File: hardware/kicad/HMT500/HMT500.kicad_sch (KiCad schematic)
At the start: 0 parts

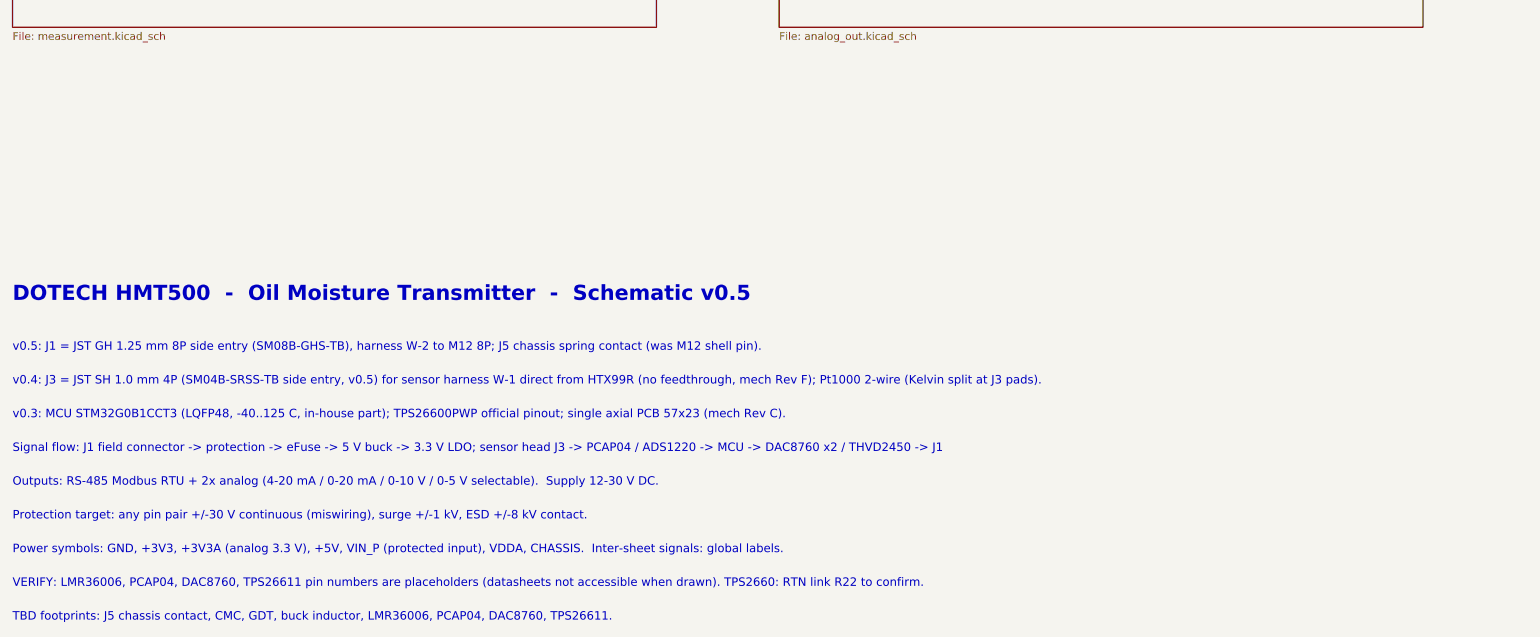
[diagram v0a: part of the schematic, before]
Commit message: Schematic drawing rules: no overlapping text, Korean font, distinct net names
- Generator places reference/value text automatically, clear of symbol bodies,
  pins, wires, labels, notes and box edges; validation fails on any overlap
  (also note text vs wires/power names and bodies vs box edges)
- Fix 180-degree parts (LED) whose justification KiCad mirrors
- Styles: reference bold, value normal, power nets italic, signal nets boxed labels
- Korean box subtitles and legend in NanumGothic TrueType (stroke font has no Hangul)
- Nets renamed where they matched part or pin names: LED -> STAT_LED, EF_ILIM/IMON/DVDT
- J1 GH mounting pads removed from the symbol (PCB only); connector sheet re-spaced
- Schematic PDF export added; tests for net naming and Hangul font

Co-Authored-By: Claude Opus 5.5 <noreply@anthropic.com>
Claude-Session: https://claude.ai/code/session_01JA2o8uJsqp9Vzsg4b665ev
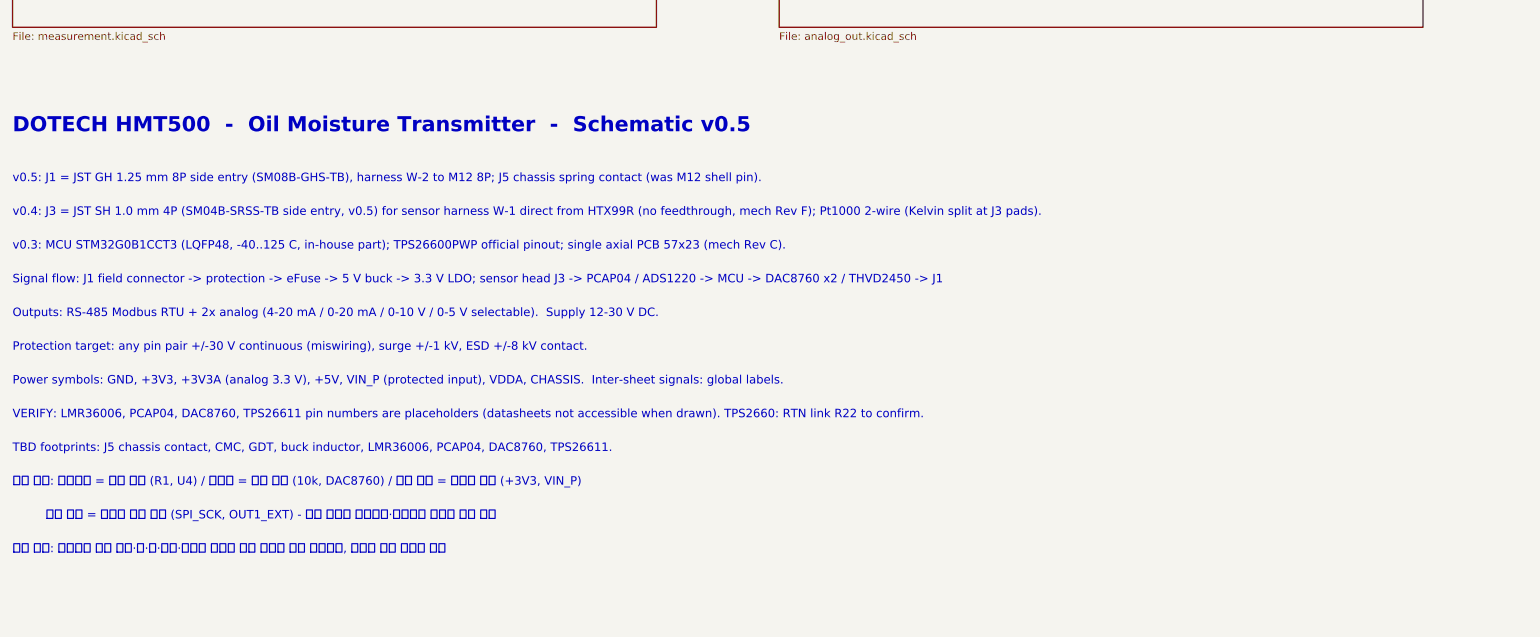
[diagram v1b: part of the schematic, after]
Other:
- note added: "글자 겹침: 생성기가 부품 몸체·핀·선·라벨·메모와 겹치지 않는 자리에 자동 배치하고, 겹치면 생성 실패로 처리"
- note added: "신호 네트 = 테두리 있는 라벨 (SPI_SCK, OUT1_EXT) - 네트 이름은 부품번호·부품명과 겹치지 않게 지음"
- note added: "표기 규칙: 부품번호 = 굵은 글자 (R1, U4) / 부품값 = 보통 글자 (10k, DAC8760) / 전원 네트 = 기울인 글자 (+3V3, VIN_P)"
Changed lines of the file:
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@@
 (sheet (at 284.48 132.08) (size 106.68 45.72) (fields_autoplaced) (stroke (width 0.1524) (type solid)) (fill (color 0 0 0 0.0000)) (property "Sheetname" "6. RS-485" (at 284.48 131.318 0) (effects (font (size 1.8 1.8) bold) (justify left bottom))) (property "Sheetfile" "rs485.kicad_sch" (at 284.48 178.562 0) (effects (font (size 1.27 1.27)) (justify left top))) (instances (project "HMT500" (path "/1ebb025b-11bd-5f7c-aaab-41e2a750e8b3" (page "7")))))
 (text "THVD2450 +/-70V fault-protected transceiver" (at 287.02 154.94 0) (effects (font (size 1.4 1.4)) (justify left bottom)))
-(text "DOTECH HMT500  -  Oil Moisture Transmitter  -  Schematic v0.5" (at 30.48 223.52 0) (effects (font (size 2.5 2.5) bold) (justify left bottom)))
-(text "v0.5: J1 = JST GH 1.25 mm 8P side entry (SM08B-GHS-TB), harness W-2 to M12 8P; J5 chassis spring contact (was M12 shell pin)." (at 30.48 231.648 0) (effects (font (size 1.4 1.4)) (justify left bottom)))
-(text "v0.4: J3 = JST SH 1.0 mm 4P (SM04B-SRSS-TB side entry, v0.5) for sensor harness W-1 direct from HTX99R (no feedthrough, mech Rev F); Pt1000 2-wire (Kelvin split at J3 pads)." (at 30.48 237.236 0) (effects (font (size 1.4 1.4)) (justify left bottom)))
-(text "v0.3: MCU STM32G0B1CCT3 (LQFP48, -40..125 C, in-house part); TPS26600PWP official pinout; single axial PCB 57x23 (mech Rev C)." (at 30.48 242.824 0) (effects (font (size 1.4 1.4)) (justify left bottom)))
-(text "Signal flow: J1 field connector -> protection -> eFuse -> 5 V buck -> 3.3 V LDO; sensor head J3 -> PCAP04 / ADS1220 -> MCU -> DAC8760 x2 / THVD2450 -> J1" (at 30.48 248.412 0) (effects (font (size 1.4 1.4)) (justify left bottom)))
-(text "Outputs: RS-485 Modbus RTU + 2x analog (4-20 mA / 0-20 mA / 0-10 V / 0-5 V selectable).  Supply 12-30 V DC." (at 30.48 254 0) (effects (font (size 1.4 1.4)) (justify left bottom)))
-(text "Protection target: any pin pair +/-30 V continuous (miswiring), surge +/-1 kV, ESD +/-8 kV contact." (at 30.48 259.588 0) (effects (font (size 1.4 1.4)) (justify left bottom)))
-(text "Power symbols: GND, +3V3, +3V3A (analog 3.3 V), +5V, VIN_P (protected input), VDDA, CHASSIS.  Inter-sheet signals: global labels." (at 30.48 265.176 0) (effects (font (size 1.4 1.4)) (justify left bottom)))
-(text "VERIFY: LMR36006, PCAP04, DAC8760, TPS26611 pin numbers are placeholders (datasheets not accessible when drawn). TPS2660: RTN link R22 to confirm." (at 30.48 270.764 0) (effects (font (size 1.4 1.4)) (justify left bottom)))
-(text "TBD footprints: J5 chassis contact, CMC, GDT, buck inductor, LMR36006, PCAP04, DAC8760, TPS26611." (at 30.48 276.352 0) (effects (font (size 1.4 1.4)) (justify left bottom)))
+(text "DOTECH HMT500  -  Oil Moisture Transmitter  -  Schematic v0.5" (at 30.48 195.58 0) (effects (font (size 2.5 2.5) bold) (justify left bottom)))
+(text "v0.5: J1 = JST GH 1.25 mm 8P side entry (SM08B-GHS-TB), harness W-2 to M12 8P; J5 chassis spring contact (was M12 shell pin)." (at 30.48 203.708 0) (effects (font (size 1.4 1.4)) (justify left bottom)))
+(text "v0.4: J3 = JST SH 1.0 mm 4P (SM04B-SRSS-TB side entry, v0.5) for sensor harness W-1 direct from HTX99R (no feedthrough, mech Rev F); Pt1000 2-wire (Kelvin split at J3 pads)." (at 30.48 209.296 0) (effects (font (size 1.4 1.4)) (justify left bottom)))
+(text "v0.3: MCU STM32G0B1CCT3 (LQFP48, -40..125 C, in-house part); TPS26600PWP official pinout; single axial PCB 57x23 (mech Rev C)." (at 30.48 214.884 0) (effects (font (size 1.4 1.4)) (justify left bottom)))
+(text "Signal flow: J1 field connector -> protection -> eFuse -> 5 V buck -> 3.3 V LDO; sensor head J3 -> PCAP04 / ADS1220 -> MCU -> DAC8760 x2 / THVD2450 -> J1" (at 30.48 220.472 0) (effects (font (size 1.4 1.4)) (justify left bottom)))
+(text "Outputs: RS-485 Modbus RTU + 2x analog (4-20 mA / 0-20 mA / 0-10 V / 0-5 V selectable).  Supply 12-30 V DC." (at 30.48 226.06 0) (effects (font (size 1.4 1.4)) (justify left bottom)))
+(text "Protection target: any pin pair +/-30 V continuous (miswiring), surge +/-1 kV, ESD +/-8 kV contact." (at 30.48 231.648 0) (effects (font (size 1.4 1.4)) (justify left bottom)))
+(text "Power symbols: GND, +3V3, +3V3A (analog 3.3 V), +5V, VIN_P (protected input), VDDA, CHASSIS.  Inter-sheet signals: global labels." (at 30.48 237.236 0) (effects (font (size 1.4 1.4)) (justify left bottom)))
+(text "VERIFY: LMR36006, PCAP04, DAC8760, TPS26611 pin numbers are placeholders (datasheets not accessible when drawn). TPS2660: RTN link R22 to confirm." (at 30.48 242.824 0) (effects (font (size 1.4 1.4)) (justify left bottom)))
+(text "TBD footprints: J5 chassis contact, CMC, GDT, buck inductor, LMR36006, PCAP04, DAC8760, TPS26611." (at 30.48 248.412 0) (effects (font (size 1.4 1.4)) (justify left bottom)))
+(text "표기 규칙: 부품번호 = 굵은 글자 (R1, U4) / 부품값 = 보통 글자 (10k, DAC8760) / 전원 네트 = 기울인 글자 (+3V3, VIN_P)" (at 30.48 254 0) (effects (font (face "NanumGothic") (size 1.4 1.4)) (justify left bottom)))
+(text "         신호 네트 = 테두리 있는 라벨 (SPI_SCK, OUT1_EXT) - 네트 이름은 부품번호·부품명과 겹치지 않게 지음" (at 30.48 259.588 0) (effects (font (face "NanumGothic") (size 1.4 1.4)) (justify left bottom)))
+(text "글자 겹침: 생성기가 부품 몸체·핀·선·라벨·메모와 겹치지 않는 자리에 자동 배치하고, 겹치면 생성 실패로 처리" (at 30.48 265.176 0) (effects (font (face "NanumGothic") (size 1.4 1.4)) (justify left bottom)))
 (sheet_instances (path "/" (page "1")))
 )
